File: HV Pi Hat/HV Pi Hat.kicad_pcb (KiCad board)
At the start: 4 copper layers, 85 x 56 mm, 47 parts, among them J3 HV_Term_1x2, J4 HV_Term_1x2, U2 MCP6001-OT

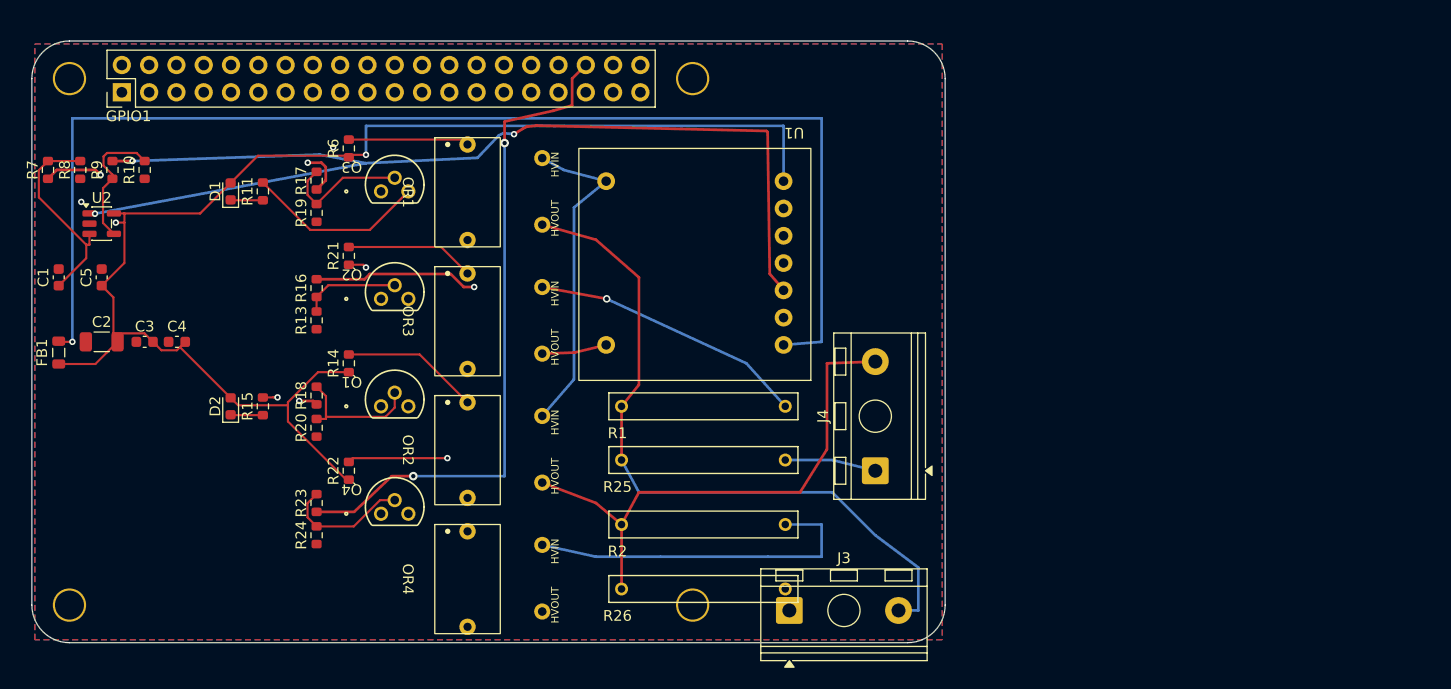
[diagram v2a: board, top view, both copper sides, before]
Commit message: Rev B: HAT+ outline board with soldered HV leads and a potted HV zone
Issue #6. Promotes the placement study (#4) to the main board:

- Schematic: J3/J4 footprint -> HV_Footprints:HV_LeadPair_P6.00mm
  (pad 1 return, pad 2 HV, 6.0 mm pitch). Netlist connectivity checked
  identical before/after (66 nets, 146 pins); ERC 0 errors.
- New footprint generated by tools/MakeLeadPair.py.
- Board: 65 x 56.5 mm HAT+ outline, study placement with J3 at the right
  edge and J4 along the bottom, pot outline + inner voids, routed by
  tools/revb/AutoRoute.py with LV kept out of the pot except over U1's
  LV pin row, GND pours on F/B.
- DRC: 0 unconnected, 0 clearance/creepage/edge errors at the 2 mm
  interim rule; schematic parity only the pre-existing D1/D2 Sim.Pins
  and H1-H4 items. Pot margin 3.00 mm. Through-board minimum 2.23 mm.
- tools/HvInterlayer.py now uses true radii for round pads.
- Docs: OPTO-100 package size corrected from the datasheet (0.40 x 0.24
  x 0.25 in), J3/J4 BOM rows, BOM.csv, CLAUDE/TOOLING/README, ADR-0004
  status, rev B renders.

Pi 5 underside keepouts are not in this commit.

Co-Authored-By: Claude Opus 5.5 <noreply@anthropic.com>
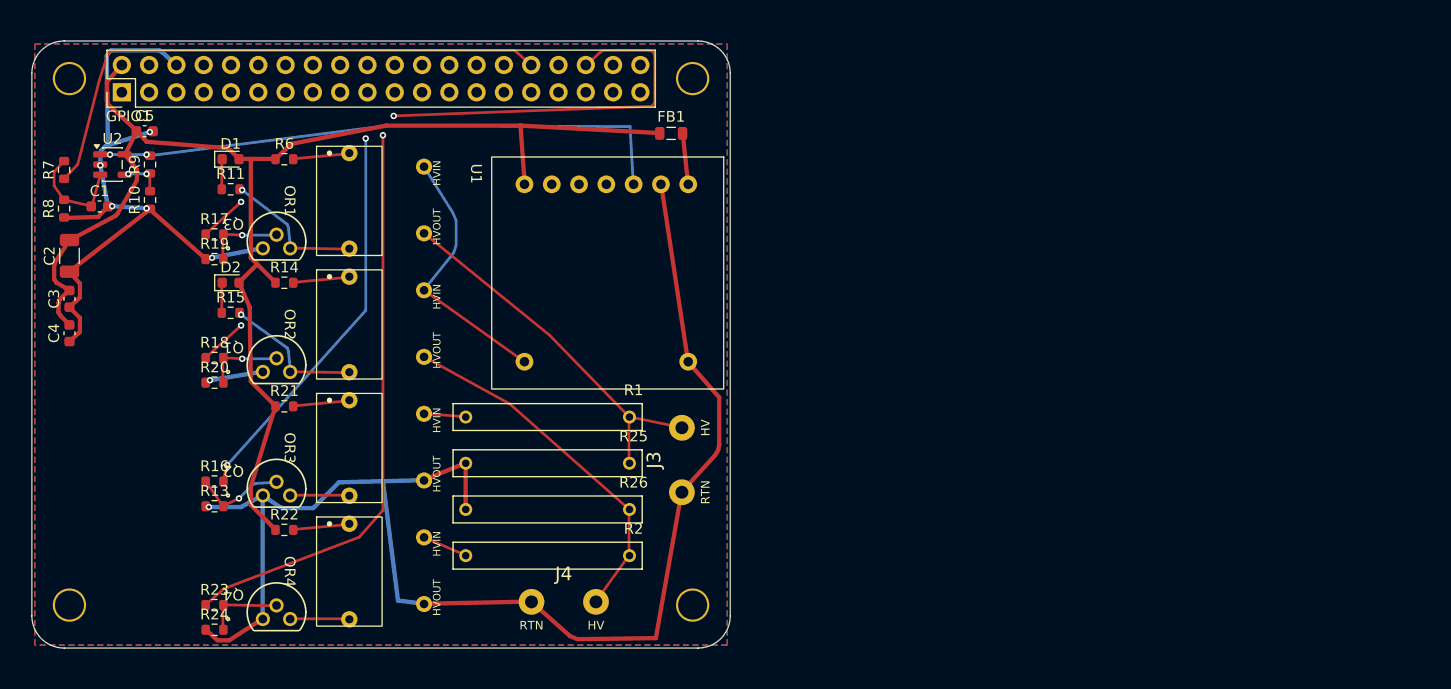
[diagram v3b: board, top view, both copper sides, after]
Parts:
- J3, J4: value HV_Term_1x2 -> HV_LeadPair; footprint TerminalBlock_RND:TerminalBlock_RND_205-00241_1x02_P10.16mm_Horizontal -> HV_Footprints:HV_LeadPair_P6.00mm
- moved FB1 60.5 mm to (177.0, 94.6), turned to 0 degrees
- moved J4 34.2 mm to (164.0, 138.2), turned to 0 degrees
- moved U1 29.7 mm to (160.3, 96.8), turned to -90 degrees
- moved Q2 21.4 mm to (139.0, 128.3)
- moved R16 20.4 mm to (134.5, 127.0), turned to 0 degrees
- moved R13 19.7 mm to (134.5, 129.3), turned to 0 degrees
- moved R26 16.3 mm to (165.5, 129.6), turned to 180 degrees
- moved OR3 16.1 mm to (144.0, 118.8)
- moved OR2 16.1 mm to (144.0, 107.3)
- moved R21 15.2 mm to (141.0, 120.0), turned to 0 degrees
- moved J3 14.9 mm to (178.0, 128.0), turned to 90 degrees
- moved R2 14.8 mm to (165.5, 133.9), turned to 180 degrees
- moved Q4 14.7 mm to (139.0, 139.8)
- moved R1 14.5 mm to (165.5, 121.0), turned to 180 degrees
- moved R25 14.5 mm to (165.5, 125.3), turned to 180 degrees
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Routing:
- net GND: track 14.5 -> 222.6 mm, vias 1 -> 7
- net Net-(U1-VIN): track 116.2 -> 4.83 mm, vias 1 -> 0
- net /GPIO_12_Boost: track 103.6 -> 54.9 mm, vias 3 -> 2
- net /HV_CH1: track 66.0 -> 35.0 mm
- net +5V: track 157.4 -> 127.7 mm, vias 3 -> 0
- net /GPIO_16: track 62.6 -> 92.2 mm
- net /HV_CH2_DIS: track 32.5 -> 4.25 mm
- net /HV_CH1_DIS: track 25.8 -> 3.91 mm, vias 1 -> 0
- net /GPIO_6: track 35.7 -> 54.2 mm, vias 1 -> 2
- net /HV_CH2: track 50.1 -> 33.5 mm
- net /CH2_CHG_DRN: track 26.3 -> 13.3 mm
- net /CH2_DIS_LED: track 16.9 -> 5.32 mm, vias 1 -> 0
- net /CH1_CHG_DRN: track 24.2 -> 13.3 mm, vias 0 -> 1
- net /PGM_IN: track 19.2 -> 9.90 mm
- net Net-(U2--): track 12.6 -> 3.92 mm, vias 0 -> 2
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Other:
- board size 85 x 56 mm -> 65 x 56.5 mm

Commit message: Rev B: 65 x 56 mm outline, hole lands, Pi 5 underside check (ADR-0005)
- Outline 65 x 56.0 mm: the legacy HAT drawing gives 56.0 for a
  through-hole GPIO header (56.5 is for SMT, extra 0.5 on the header
  edge); the study's 56.5 had the extra on the wrong edge. J4 moved up
  0.4 mm to keep its 3 mm pot margin.
- 6.2 mm copper-free land around each mounting hole (HAT drawing).
- Left-edge strip kept free so a PCIe flex notch stays possible; C2-C4
  moved off it.
- tools/revb/PiKeepouts.py: Pi 5 parts from the official drawings drawn
  on User.2, with the vertical room at a given standoff. At 16 mm the
  Active Cooler (13.70 mm worst case) collides with the 3 mm bottom pot
  by 0.7 mm; at 20 mm there is 3.3 mm. USB-A/RJ45 are outside the 65 mm
  outline. ADR-0005 (Proposed) records this, plus the GPIO socket
  (8.51 mm body) that cannot give either gap.
- Header GND pins get solid zone connections (starved thermal).

DRC: 0 unconnected, 0 electrical errors; parity unchanged from rev A
(D1/D2 Sim.Pins, H1-H4). ERC 0 errors. Pot margin 3.00 mm.

Co-Authored-By: Claude Opus 5.5 <noreply@anthropic.com>
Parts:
- moved C2 3.60 mm to (124.6, 106.0)
- moved C3 3.60 mm to (124.6, 110.0)
- moved C4 3.60 mm to (124.6, 113.2)
- moved J4 0.40 mm to (164.0, 137.8)
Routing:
- net GND: track 222.6 -> 216.4 mm, vias 7 -> 8
- net +5V: track 127.7 -> 125.2 mm
- net /GPIO_12: vias 0 -> 1
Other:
- board size 65 x 56.5 mm -> 65 x 56 mm
- board text added: "Pi5 ActiveCooler h 13.7"
- board text added: "Pi5 CoolerFan h 13.7"
- board text added: "Pi5 FPC_A h 4.1"
- board text added: "Pi5 FPC_B h 4.1"
- board text added: "Pi5 PCIe_FFC h 4.2"
- board text added: "Pi5 PoE h 8.6"
- board text added: "Pi5 RTC_J5 h 4.5"
- board text added: "Pi5 UART h 4.4"

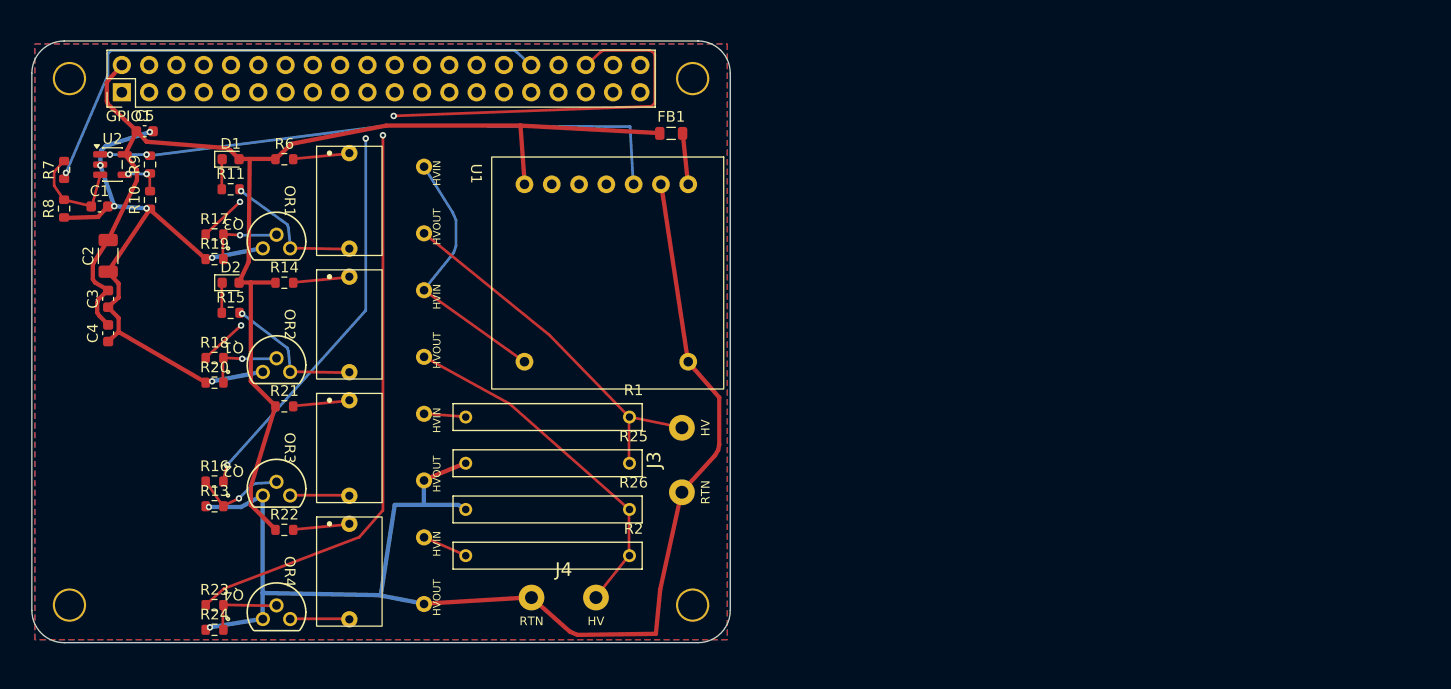
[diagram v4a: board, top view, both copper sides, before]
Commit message: Rev B: opto drive, ID EEPROM, underside socket, NPTH holes, bench plan
Implements the recommendations from the 2026-10-08 decision list:

- ADR-0006: opto LED resistors R6/R14/R21/R22 51 Ohm 0603 -> 15 Ohm
  1206. The OPTO-100 datasheet's CTR graph starts at about 40 mA of
  LED current; 51 Ohm gave about 38 mA. 15 Ohm gives about 110 mA.
- ADR-0007: HAT+ ID EEPROM (CAT24C32 at 0x50, 3.9k ID pull-ups, 1k WP
  pull-up + TP1, 100 nF) added to the schematic by
  tools/revb/AddIdEeprom.py; netlist checked: only the four new nets
  (+3V3, ID_SD, ID_SC, ID_WP) and GND gained pins, everything else
  identical. GPIO1 becomes a bottom-side 2x20 socket (pads verified
  identical); H1-H4 become unplated 2.75 mm holes.
- tools/revb/BuildRevB.py now syncs the board from the schematic
  netlist (footprint swaps, new parts, every pad net).
- docs/BENCH_TESTS.md: T1-T9, including an opto HV lead polarity check
  (a reversed photodiode conducts with no light).
- Docs: CONTROL_DESIGN, CLAUDE, datasheets README correction, BOM.

ERC 0 errors (8 warnings, 7 pre-existing). DRC 0 unconnected, 0
electrical; parity 6 pre-existing (D1/D2 Sim.Pins, H1-H4). Pot margin
3.00 mm, through-board 2.23 mm, Active Cooler room 3.3 mm at 20 mm.

Co-Authored-By: Claude Opus 5.5 <noreply@anthropic.com>
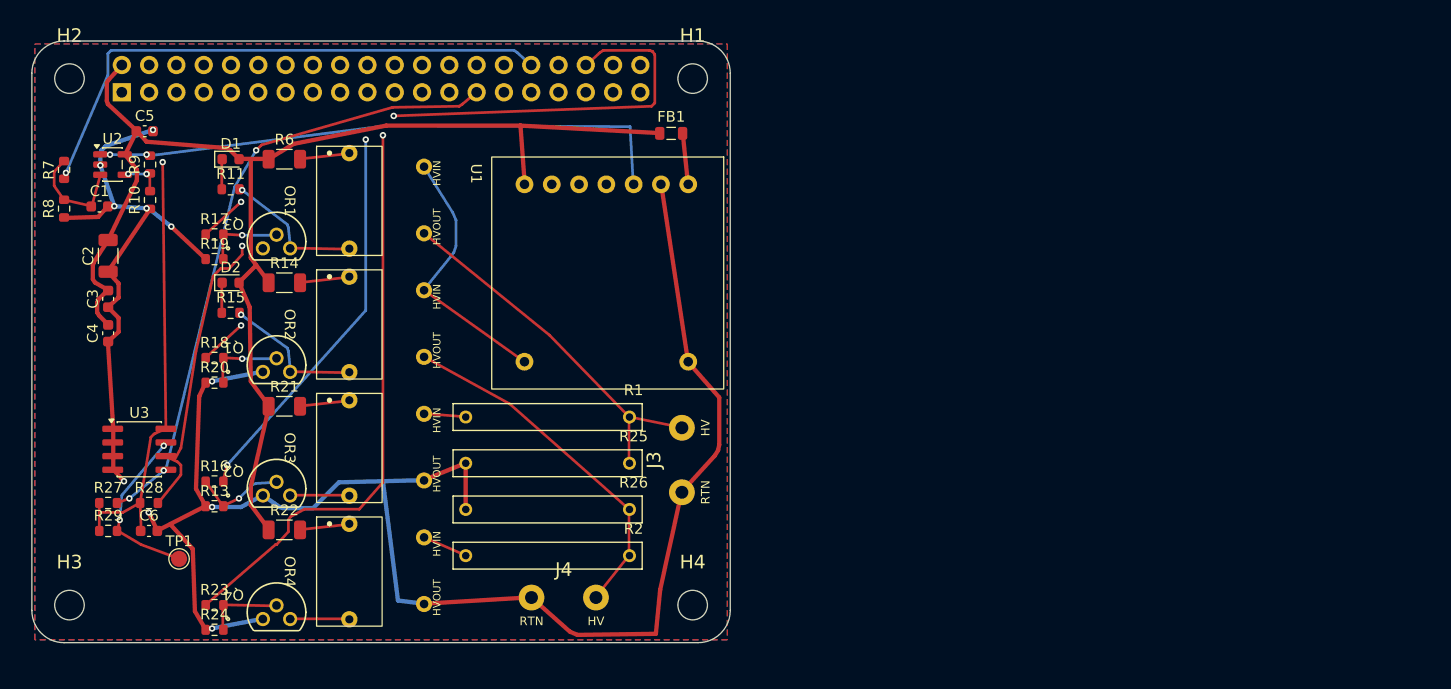
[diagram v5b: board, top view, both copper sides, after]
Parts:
- added C6: 0.1 uF, Capacitor_SMD:C_0603_1608Metric, F.Cu at (128.4, 131.6)
- added R27: 3.9k, Resistor_SMD:R_0603_1608Metric, F.Cu at (124.6, 129.0)
- added R28: 3.9k, Resistor_SMD:R_0603_1608Metric, F.Cu at (128.4, 129.0)
- added R29: 1k, Resistor_SMD:R_0603_1608Metric, F.Cu at (124.6, 131.6)
- added TP1: ID_WP, TestPoint:TestPoint_Pad_D1.5mm, F.Cu at (131.2, 134.2)
- added U3: CAT24C32, Package_SO:SOIC-8_3.9x4.9mm_P1.27mm, F.Cu at (127.5, 124.0)
- GPIO1: value ~ -> Samtec ESQ-120-14-G-D; footprint Connector_PinHeader_2.54mm:PinHeader_2x20_P2.54mm_Vertical -> Connector_PinSocket_2.54mm:PinSocket_2x20_P2.54mm_Vertical; moved to B.Cu
- H1, H2, H3, H4: value MountingHole_2.7mm_M2.5_Pad_TopBottom -> MountingHole_2.75mm_M2.5_NPTH_HAT; footprint MountingHole:MountingHole_2.7mm_M2.5_Pad_TopBottom -> HV_Footprints:MountingHole_2.75mm_M2.5_NPTH_HAT
- R14, R21, R22, R6: value 51 -> 15; footprint Resistor_SMD:R_0603_1608Metric -> Resistor_SMD:R_1206_3216Metric
- turned GPIO1 to -90 degrees
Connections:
- GPIO1 pad 1: unconnected-(GPIO1-3.3V-Pad1) -> +3V3
- GPIO1 pad 27: unconnected-(GPIO1-GPIO_0-Pad27) -> /ID_SD
- GPIO1 pad 28: unconnected-(GPIO1-GPIO_1-Pad28) -> /ID_SC
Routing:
- net /ID_SD: track 0.00 -> 58.2 mm, vias 0 -> 3
- net /ID_SC: track 0.00 -> 57.9 mm, vias 0 -> 1
- net +3V3: track 0.00 -> 49.4 mm, vias 0 -> 1
- net GND: track 216.4 -> 236.7 mm, vias 8 -> 10
- net /ID_WP: track 0.00 -> 16.0 mm, vias 0 -> 2
- net +5V: track 125.2 -> 123.5 mm
- net Net-(OR1-LED+): track 5.32 -> 4.63 mm
- net /CH2_DIS_LED: track 5.32 -> 4.63 mm
- net /CH2_CHG_LED: track 5.32 -> 4.63 mm
- net /CH1_DIS_LED: track 5.32 -> 4.63 mm
